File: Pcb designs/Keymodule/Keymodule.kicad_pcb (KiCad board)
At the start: 4 copper layers, 91 x 91 mm, 113 parts, among them J1 USB connect, U1 RP2040, U2 SN74LV1T34DBV, U3 AMS1117-3.3, U4 W25Q128JVS, Y1 ABM8-272-T3

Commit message: Almost done
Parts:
- removed JIn1: Conn_01x05, Connector_PinSocket_2.00mm:PinSocket_1x05_P2.00mm_Horizontal
- removed JOut1: Conn_01x05, 1_Custom_library:Magnetic pogo out
- removed REF** (x4): PinHeader_1x01_P1.27mm_Horizontal, Connector_PinHeader_1.27mm:PinHeader_1x01_P1.27mm_Horizontal
- removed REF** (x3): TestPoint_Pad_1.0x1.0mm, TestPoint:TestPoint_Pad_1.0x1.0mm
- removed REF**: PinHeader_1x03_P1.27mm_Horizontal, Connector_PinHeader_1.27mm:PinHeader_1x03_P1.27mm_Horizontal
- added J11: USB connect, Connector_PinSocket_2.54mm:PinSocket_1x05_P2.54mm_Vertical, F.Cu at (33.1, 150.8)
- added J2: Conn_01x01, Connector_PinHeader_1.27mm:PinHeader_1x01_P1.27mm_Horizontal, F.Cu at (60.4, 109.5)
- added J3: Conn_01x03, Connector_PinHeader_1.27mm:PinHeader_1x03_P1.27mm_Horizontal, F.Cu at (72.1, 101.1)
- added J4: Conn_01x01, Connector_PinHeader_1.27mm:PinHeader_1x01_P1.27mm_Horizontal, F.Cu at (139.6, 90.5)
- added J5: Conn_01x01, Connector_PinHeader_1.27mm:PinHeader_1x01_P1.27mm_Horizontal, F.Cu at (139.6, 109.5)
- added J6: Conn_01x03, Connector_PinHeader_1.27mm:PinHeader_1x03_P1.27mm_Horizontal, B.Cu at (128.2, 101.7)
- J1: value USB connect -> Conn_01x01; footprint Connector_PinSocket_2.54mm:PinSocket_1x05_P2.54mm_Vertical -> Connector_PinHeader_1.27mm:PinHeader_1x01_P1.27mm_Horizontal
- moved R4 98.1 mm to (91.4, 78.2), turned to 45 degrees
- moved J1 82.4 mm to (60.4, 90.5), turned to 180 degrees
- moved TP2 8.67 mm to (71.4, 57.5)
- moved TP1 6.10 mm to (98.1, 77.8)
- moved D19 3.86 mm to (78.1, 74.9), turned to 180 degrees
- moved R3 0.40 mm to (100.5, 73.2)
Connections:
- net Net-(U1-GPIO15) renamed /ledDataOut
- net Net-(U1-RUN) renamed /run
- net ledData renamed WS2812bData
- J1 pad 1: GND -> +5V
- R6 pad 2: Net-(J1-Pin_3) -> Net-(J11-Pin_3)
- R7 pad 2: Net-(J1-Pin_4) -> Net-(J11-Pin_4)
- U1 pad 11: col2 -> row2
- U1 pad 12: col3 -> row1
- U1 pad 13: col4 -> row0
- U1 pad 2: row0 -> col0
- U1 pad 3: row1 -> col1
- U1 pad 4: row2 -> col2
- U1 pad 5: row3 -> col3
- U1 pad 6: row4 -> col4
- U1 pad 8: col0 -> row4
- U1 pad 9: col1 -> row3
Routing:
- net GND: track 710.6 -> 795.3 mm, vias 12 -> 16
- net col4: track 76.0 -> 149.8 mm, vias 0 -> 1
- net row0: track 77.8 -> 139.2 mm, vias 6 -> 7
- net col3: track 76.0 -> 130.8 mm, vias 0 -> 1
- net col1: track 38.0 -> 92.1 mm, vias 0 -> 1
- net row1: track 78.4 -> 124.5 mm, vias 6 -> 8
- net col2: track 76.0 -> 110.9 mm, vias 0 -> 1
- net col0: track 57.0 -> 90.4 mm, vias 0 -> 1
- net row2: track 81.6 -> 105.8 mm, vias 6 -> 7
- net row4: track 77.3 -> 101.6 mm, vias 6 -> 7
- net Net-(L3-DOUT): track 0.00 -> 15.6 mm, vias 0 -> 2
- net Net-(L2-DOUT): track 1.79 -> 15.5 mm, vias 1 -> 2
- net Net-(R2-Pad1): track 0.00 -> 13.1 mm
- net +3.3V: track 34.5 -> 47.3 mm
- net /run: track 8.16 -> 16.2 mm
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
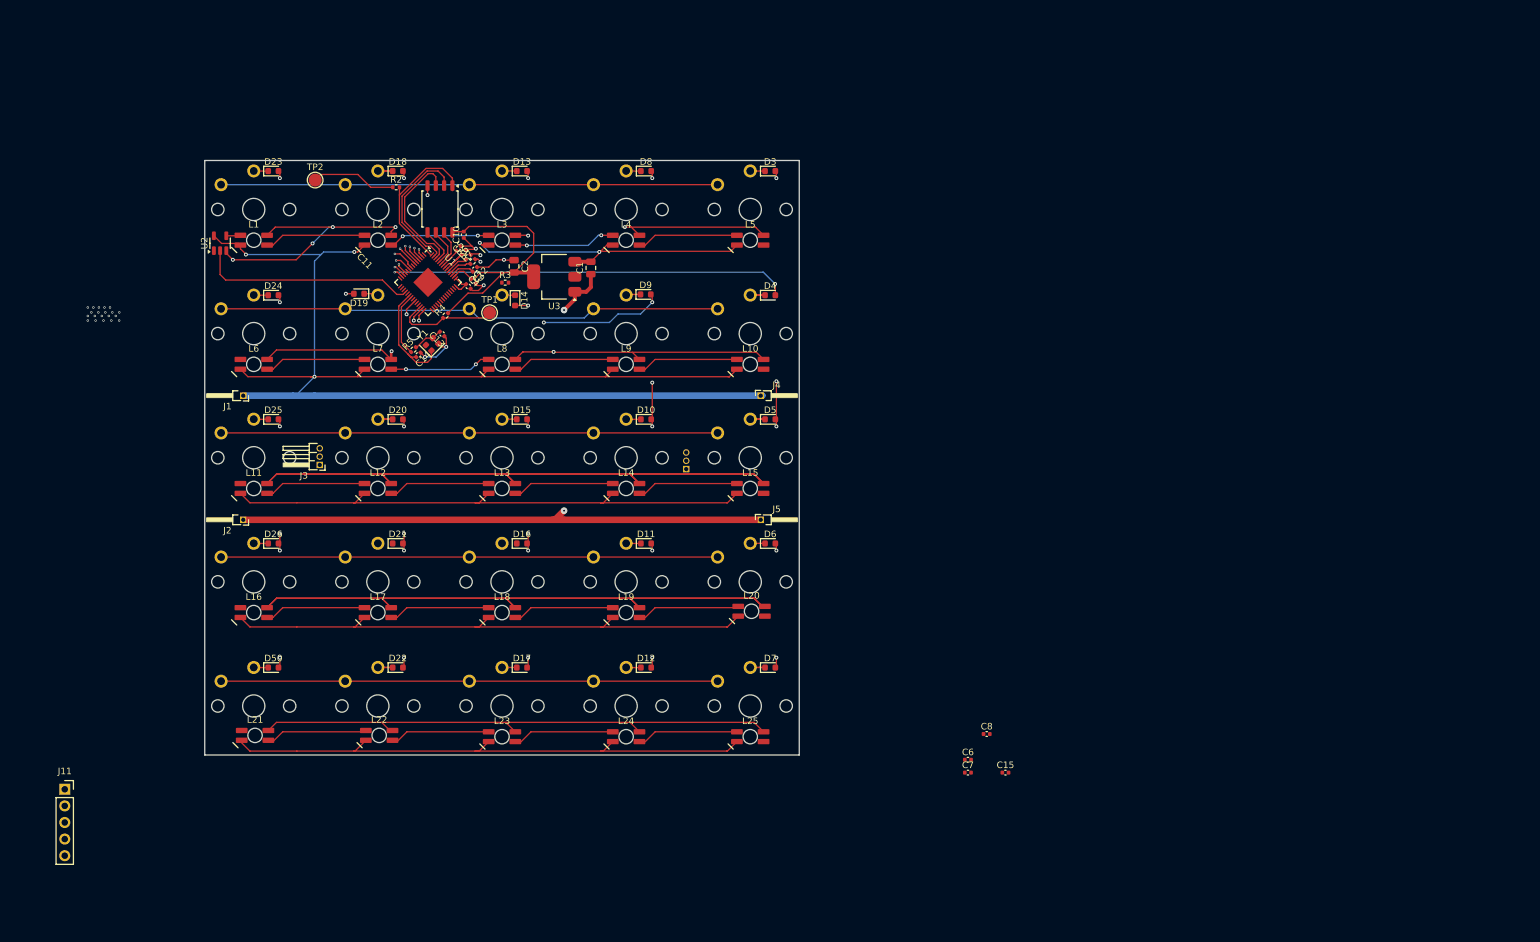
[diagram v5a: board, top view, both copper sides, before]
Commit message: Led's & buttons are done
Still need to optimize and check MCU connections
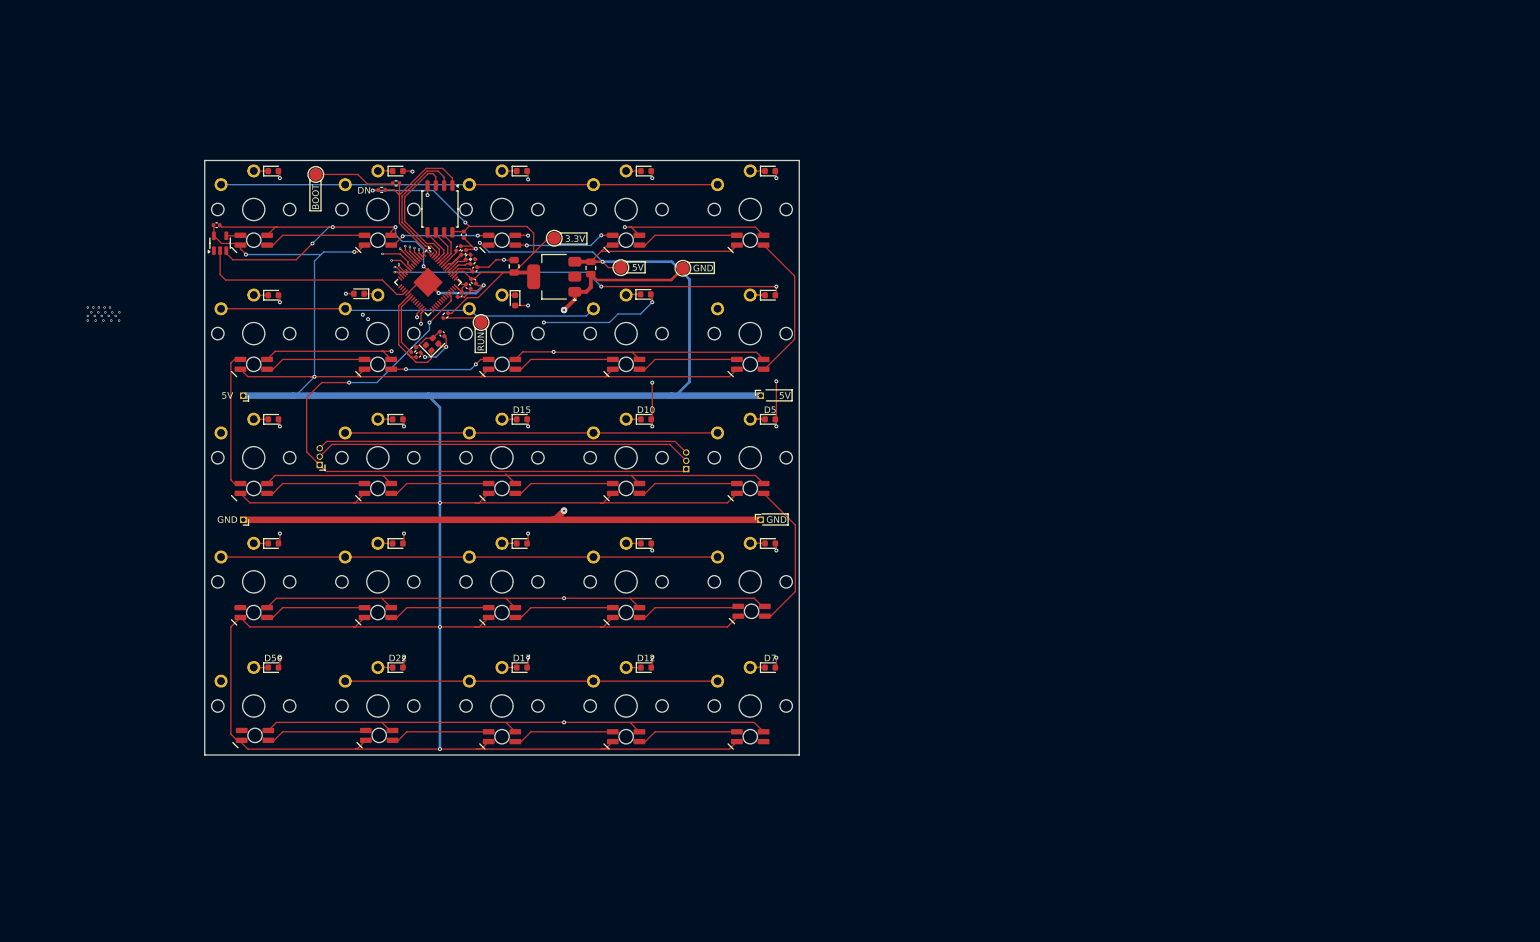
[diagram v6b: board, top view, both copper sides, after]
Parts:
- removed C6, C7: 100nf, Capacitor_SMD:C_0402_1005Metric
- removed J11: USB connect, Connector_PinSocket_2.54mm:PinSocket_1x05_P2.54mm_Vertical
- added 3.3V: TestPoint_Pad_D2.0mm, TestPoint:TestPoint_Pad_D2.0mm, F.Cu at (108.0, 66.4)
- added 5V: TestPoint_Pad_D2.0mm, TestPoint:TestPoint_Pad_D2.0mm, F.Cu at (118.2, 70.9)
- added GND: TestPoint_Pad_D2.0mm, TestPoint:TestPoint_Pad_D2.0mm, F.Cu at (127.7, 71.0)
- DN: renamed from R3; value 1K -> 10K DNF
- R2: value 10K -> 1K
- moved C15 147.0 mm to (56.3, 64.4)
- moved C8 105.0 mm to (93.6, 75.0), turned to -135 degrees
- moved DN 23.6 mm to (81.6, 59.0), turned to 180 degrees
- moved RUN 1.98 mm to (96.8, 79.3)
- moved BOOT 0.87 mm to (71.5, 56.6)
- moved R2 0.60 mm to (83.8, 58.0)
- renumbered J4 to 5V, J1 to 5V, TP2 to BOOT, J5 to GND, J2 to GND, TP1 to RUN
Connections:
- L11 pad 4: Net-(L10-DOUT) -> Net-(L11-DIN)
- L16 pad 4: Net-(L15-DOUT) -> Net-(L16-DIN)
- L20 pad 2: Net-(L20-DOUT) -> Net-(L15-DOUT)
- L21 pad 4: Net-(L20-DOUT) -> Net-(L16-DIN)
- L5 pad 2: Net-(L5-DOUT) -> Net-(L10-DOUT)
- L6 pad 4: Net-(L5-DOUT) -> Net-(L11-DIN)
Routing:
- net +5V: track 513.7 -> 627.4 mm, vias 5 -> 8
- net potSig: track 0.00 -> 97.5 mm, vias 0 -> 2
- net SDA: track 2.79 -> 94.1 mm, vias 1 -> 2
- net SCL: track 1.90 -> 90.7 mm, vias 1 -> 2
- net Net-(L15-DOUT): track 0.00 -> 23.3 mm
- net Net-(L10-DOUT): track 0.00 -> 22.9 mm
- net Net-(L11-DIN): track 0.00 -> 21.3 mm
- net +3.3V: track 47.3 -> 67.8 mm, vias 0 -> 2
- net row3: track 74.7 -> 94.5 mm, vias 7 -> 6
- net GND: track 795.3 -> 782.9 mm, vias 16 -> 19
- net /run: track 16.2 -> 6.30 mm
- net row2: track 105.8 -> 114.4 mm, vias 7 -> 6
- net Net-(U1-QSPI_SS): track 23.8 -> 26.7 mm
- net +1V1: track 9.24 -> 6.68 mm, vias 1 -> 0
- net Net-(D22-K): track 4.51 -> 2.24 mm
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
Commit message: Better final version
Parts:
- added DN: 1K, Resistor_SMD:R_0402_1005Metric, F.Cu at (96.8, 61.6)
- added REF**: MountingHole_2.2mm_M2, MountingHole:MountingHole_2.2mm_M2, F.Cu at (128.5, 128.5)
- added REF**: PinHeader_1x05_P2.54mm_Vertical, Connector_PinHeader_2.54mm:PinHeader_1x05_P2.54mm_Vertical, F.Cu at (128.6, 66.4)
- added REF**: MountingHole_2.2mm_M2, MountingHole:MountingHole_2.2mm_M2, F.Cu at (71.5, 128.5)
- added REF**: MountingHole_2.2mm_M2, MountingHole:MountingHole_2.2mm_M2, F.Cu at (71.5, 71.5)
- added REF**: MountingHole_2.2mm_M2, MountingHole:MountingHole_2.2mm_M2, F.Cu at (128.5, 71.5)
- J3, J6: footprint Connector_PinHeader_1.27mm:PinHeader_1x03_P1.27mm_Horizontal -> Connector_PinHeader_2.54mm:PinHeader_1x03_P2.54mm_Horizontal
- R2: value 1K -> 10K
- moved GND 43.9 mm to (111.7, 111.9)
- moved R6 32.6 mm to (126.3, 61.0), turned to -90 degrees
- moved R7 30.9 mm to (125.8, 63.8), turned to 0 degrees
- moved C15 7.54 mm to (58.3, 71.7), turned to 90 degrees
- moved 5V 7.50 mm to (67.9, 90.5)
- moved U2 6.00 mm to (61.2, 71.2), turned to 180 degrees
- moved D14 1.84 mm to (100.8, 77.3), turned to 0 degrees
- moved J3 1.58 mm to (71.5, 102.6)
- moved C2 1.35 mm to (101.9, 72.0)
- moved J6 0.87 mm to (128.5, 102.6)
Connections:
- U1 pad 11: row2 -> col2
- U1 pad 12: row1 -> col3
- U1 pad 13: row0 -> col4
- U1 pad 2: col0 -> row1
- U1 pad 3: col1 -> row0
- U1 pad 37: unconnected-(U1-GPIO25-Pad37) -> potSig
- U1 pad 4: col2 -> col1
- U1 pad 5: col3 -> row2
- U1 pad 6: col4 -> row3
- U1 pad 8: row4 -> col0
- U1 pad 9: row3 -> row4
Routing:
- net potSig: track 97.5 -> 40.7 mm
- net USB_D+: track 3.38 -> 43.1 mm, vias 0 -> 2
- net USB_D-: track 3.63 -> 39.2 mm, vias 0 -> 2
- net +5V: track 627.4 -> 604.0 mm, vias 8 -> 9
- net Net-(L16-DIN): track 0.90 -> 20.4 mm
- net GND: track 782.9 -> 766.1 mm, vias 19 -> 18
- net /ledDataOut: track 33.5 -> 25.6 mm
- net Net-(U1-QSPI_SS): track 26.7 -> 32.6 mm
- net WS2812bData: track 2.09 -> 7.49 mm
- net col0: track 90.4 -> 95.6 mm
- net col4: track 149.8 -> 144.7 mm
- net row0: track 137.3 -> 141.9 mm, vias 8 -> 7
- net row3: track 94.5 -> 99.0 mm
- net col3: track 130.8 -> 126.6 mm
- net col2: track 110.9 -> 108.0 mm
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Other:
- board text added: "+"
- board text added: "-"
- board text added: "5V"
- board text added: "G"
- board text added: "Keymodule V1.1"

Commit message: Backup before auto cleanup
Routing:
- net row0: track 141.9 -> 143.9 mm, vias 7 -> 6
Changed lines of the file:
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@@
+	)
+	(segment
+		(start 142 95.2)
+		(end 142 94.2825)
+		(width 0.2)
+		(layer "F.Cu")
+		(net 9)
 	)
 	(segment
@@
 	)
 	(segment
-		(start 142 94.27)
-		(end 142 94.9)
-		(width 0.2)
-		(layer "F.Cu")
-		(net 9)
-	)
-	(segment
 		(start 86.554477 68.095526)
 		(end 86.554477 68.485881)
@@
 	)
 	(segment
-		(start 142 88.3)
-		(end 142 93.97)
-		(width 0.2)
-		(layer "F.Cu")
-		(net 9)
-	)
-	(segment
 		(start 142 56.27)
-		(end 142 56.9)
+		(end 142 57.2)
+		(width 0.2)
+		(layer "F.Cu")
+		(net 9)
+	)
+	(segment
+		(start 142 94.2825)
+		(end 141.8375 94.12)
 		(width 0.2)
 		(layer "F.Cu")
@@
 	(via
 		(at 142 130.6)
-		(size 0.6)
+		(size 0.4)
 		(drill 0.3)
 		(layers "F.Cu" "B.Cu")
@@
 	(via
 		(at 142 57.2)
-		(size 0.6)
-		(drill 0.3)
-		(layers "F.Cu" "B.Cu")
-		(net 9)
-	)
-	(via
-		(at 142 88.3)
-		(size 0.6)
+		(size 0.4)
 		(drill 0.3)
 		(layers "F.Cu" "B.Cu")
@@
 	(via
 		(at 142 114.2)
-		(size 0.6)
+		(size 0.4)
 		(drill 0.3)
 		(layers "F.Cu" "B.Cu")
@@
 	(via
 		(at 142 95.2)
-		(size 0.6)
+		(size 0.4)
 		(drill 0.3)
 		(layers "F.Cu" "B.Cu")
@@
 	(via
 		(at 142 73.2)
-		(size 0.6)
-		(drill 0.3)
-		(layers "F.Cu" "B.Cu")
+		(size 0.4)
+		(drill 0.3)
+		(layers "F.Cu" "B.Cu")
+		(net 9)
+	)
+	(segment
+		(start 142 95.2)
+		(end 142 57.2)
+		(width 0.2)
+		(layer "B.Cu")
+		(net 9)
+	)
+	(segment
+		(start 142 95.2)
+		(end 142 114.2)
+		(width 0.2)
+		(layer "B.Cu")
+		(net 9)
+	)
+	(segment
+		(start 142 114.2)
+		(end 142 130.6)
+		(width 0.2)
+		(layer "B.Cu")
 		(net 9)
 	)
@@
 	)
 	(segment
-		(start 142 95.2)
-		(end 142 114.2)
-		(width 0.2)
-		(layer "In1.Cu")
-		(net 9)
-	)
-	(segment
 		(start 142 73.2)
 		(end 142 74.099999)
@@
 	)
 	(segment
-		(start 142 57.2)
-		(end 142 88.3)
-		(width 0.2)
-		(layer "In1.Cu")
-		(net 9)
-	)
-	(segment
 		(start 96.6 76.9)
 		(end 88.4 68.7)
-		(width 0.2)
-		(layer "In1.Cu")
-		(net 9)
-	)
-	(segment
-		(start 142 114.2)
-		(end 142 130.6)
 		(width 0.2)
 		(layer "In1.Cu")
@@
 	)
 	(segment
+		(start 127.878 97.7)
+		(end 72.122 97.7)
+		(width 0.4)
+		(layer "F.Cu")
+		(net 41)
+	)
+	(segment
 		(start 128.5 97.48)
 		(end 128.079 97.901)
@@
 	(segment
 		(start 128.079 97.901)
-		(end 71.921 97.901)
-		(width 0.2)
+		(end 127.878 97.7)
+		(width 0.4)
 		(layer "F.Cu")
 		(net 41)
@@
 		(end 87.6 78.8)
 		(width 0.2)
+		(layer "F.Cu")
+		(net 41)
+	)
+	(segment
+		(start 72.122 97.7)
+		(end 71.921 97.901)
+		(width 0.4)
 		(layer "F.Cu")
 		(net 41)
@@
 	)
 	(segment
-		(start 71.5 100.02)
-		(end 73.481 102.001)
-		(width 0.2)
-		(layer "F.Cu")
-		(net 42)
-	)
-	(segment
-		(start 126.519 102.001)
-		(end 128.5 100.02)
-		(width 0.2)
-		(layer "F.Cu")
-		(net 42)
-	)
-	(segment
 		(start 86.5 78.5)
 		(end 86.5 78.4)
@@
 	)
 	(segment
-		(start 73.481 102.001)
-		(end 126.519 102.001)
-		(width 0.2)
+		(start 126.32 102.2)
+		(end 128.5 100.02)
+		(width 0.4)
 		(layer "F.Cu")
 		(net 42)
+	)
+	(segment
+		(start 73.68 102.2)
+		(end 126.32 102.2)
+		(width 0.4)
+		(layer "F.Cu")
+		(net 42)
+	)
+	(segment
+		(start 71.5 100.02)
+		(end 73.68 102.2)
+		(width 0.4)
+		(layer "F.Cu")
+		(net 42)
